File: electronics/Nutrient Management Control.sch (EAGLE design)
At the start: 28 parts, among them IC1 7407N, K1 SRM-1C-SL-5VDC, Q1 FQP30N06L, Q2 FQP30N06L, Q6 FDU3N40TU

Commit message: Just Microcontroller and control signals left todo
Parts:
- removed 24ACVS, IPUMP: (no value), Aeroponics Control:HEADER_POS2_43650-0215
- removed FM1, PS1: JST-XH-03-PIN-LONG-PAD, Aeroponics Control:JST-XH-03-PIN-LONG-PAD
- removed IPRSV, ISV: JST-XH-02-PIN-LONG-PAD, Aeroponics Control:JST-XH-02-PIN-LONG-PAD
- added C2, C3: 100n, Aeroponics Control:C-EU050-024X044
- added D10, D11, D12, D13, D14, D3, D4, D5, D7, D8, D9: 1N4004, Aeroponics Control:1N4004
- added DS4, DS5, ISEC: JST-XH-04-PIN-LONG-PAD, Aeroponics Control:JST-XH-04-PIN-LONG-PAD
- added HEAT, UV: (no value), Aeroponics Control:HEADER_POS2_43650-0215
- added IC2, IC3: 7407N, Aeroponics Control:7407N
- added K2: SRM-1C-SL-5VDC, Aeroponics Control:SRM-1C-SL-5VDC
- added MIXP, NP1, NP2, NP3, NP4, NP5, NP6, NP7, NP8, RORP, SUPP, WV: JST-XH-02-PIN-LONG-PAD, Aeroponics Control:JST-XH-02-PIN-LONG-PAD
- added Q10, Q11, Q12, Q13, Q3, Q4, Q5, Q7, Q8, Q9: FQP30N06L, Aeroponics Control:FQP30N06L
- added Q14: FDU3N40TU, Aeroponics Control:FDU3N40TU
- added R10, R13, R15, R17, R19, R21, R23, R25, R27, R3, R7: 10k, Aeroponics Control:R-EU_0204/7
- added R12, R14, R16, R18, R20, R22, R24, R26, R28, R4, R9: 1K, Aeroponics Control:R-EU_0204/7
- added TDS1, TDS2, TS1: JST-XH-03-PIN-LONG-PAD, Aeroponics Control:JST-XH-03-PIN-LONG-PAD
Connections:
- removed net +24VAC: 24ACVS.1, K1.COM
- removed net -24VAC: 24ACVS.2, IPUMP.1
- new net N$11: D4.A, NP3-2.S, Q4.D
- new net N$12: IC1C.O, R7.1, R9.1
- new net N$14: Q4.G, R9.2
- new net N$15: D5.A, NP5-2.S, Q5.D
- new net N$16: IC1E.O, R10.1, R12.1
- new net N$18: Q5.G, R12.2
- new net N$19: D7.A, NP7-2.S, Q7.D
- new net N$2: D3.A, NP1-2.S, Q3.D
- new net N$20: IC2A.O, R13.1, R14.1
- new net N$22: Q7.G, R14.2
- new net N$23: D8.A, NP2-2.S, Q8.D
- new net N$24: IC1B.O, R15.1, R16.1
- new net N$25: Q8.G, R16.2
- new net N$26: D9.A, NP4-2.S, Q9.D
- new net N$27: IC1D.O, R17.1, R18.1
- new net N$28: Q9.G, R18.2
- new net N$29: D10.A, NP6-2.S, Q10.D
- new net N$30: IC1F.O, R19.1, R20.1
- new net N$31: Q10.G, R20.2
- new net N$32: D11.A, NP8-2.S, Q11.D
- new net N$33: IC2B.O, R21.1, R22.1
- new net N$34: Q11.G, R22.2
- new net N$35: D12.A, Q12.D, RORP-2.S
- new net N$36: IC2E.O, R23.1, R24.1
- new net N$37: Q12.G, R24.2
- new net N$38: D13.A, Q13.D, WV-2.S
- new net N$39: IC2F.O, R25.1, R26.1
- new net N$40: Q13.G, R26.2
- new net N$41: D14.A, K2.COIL_1, Q14.D
- new net N$42: HEAT.2, K2.NO
- new net N$43: Q14.G, R28.2
- new net N$44: IC3B.O, R27.1, R28.1
- new net N$47: DS4-3.S
- new net N$48: DS4-4.S
- new net N$49: DS5-3.S
- new net N$50: DS5-4.S
- new net N$6: IC1A.O, R3.1, R4.1
- new net N$8: Q3.G, R4.2
- net +12V: now also D10.C, D11.C, D12.C, D13.C, D3.C, D4.C, D5.C, D7.C, D8.C, D9.C, MIXP-1.S, NP1-1.S, NP2-1.S, NP3-1.S, NP4-1.S, NP5-1.S, NP6-1.S, NP7-1.S, NP8-1.S, R27.2, RORP-1.S, SUPP-1.S, WV-1.S; no longer IPRSV-1.S, ISV-1.S
- net +240VAC: now also K1.COM, K2.COM
- net +5V: now also C2.1, C3.1, D14.C, DS4-1.S, DS5-1.S, IC2P.VCC, IC3P.VCC, K2.COIL_2, R10.2, R13.2, R15.2, R17.2, R19.2, R21.2, R23.2, R25.2, R3.2, R7.2, TDS1-1.S, TDS2-1.S, TS1-1.S; no longer FM1-1.S, PS1-1.S
- net -240VAC: now also HEAT.1, UV.1
- net DS1RX: no longer DS1-3.S
- net DS1TX: no longer DS1-4.S
- net DS2RX: no longer DS2-3.S
- net DS2TX: no longer DS2-4.S
- net DS3RX: no longer DS3-3.S
- net DS3TX: no longer DS3-4.S
- net FM1S: no longer FM1-3.S
- net GND: now also C2.2, C3.2, DS4-2.S, DS5-2.S, IC2P.GND, IC3P.GND, Q10.S, Q11.S, Q12.S, Q13.S, Q14.S, Q3.S, Q4.S, Q5.S, Q7.S, Q8.S, Q9.S, TDS1-2.S, TDS2-2.S, TS1-2.S; no longer FM1-2.S, PS1-2.S
- net IPCTL: no longer IC1E.I
- net IPRSVCTL: no longer IC1B.I
- net ISVCTL: no longer IC1A.I
- net N$1: now also MIXP-2.S; no longer IPRSV-2.S
- net N$10: now also SUPP-2.S; no longer ISV-2.S
- net N$17: now also IC3A.O; no longer IC1E.O
- net N$3: now also IC2D.O; no longer IC1A.O
- net N$7: now also UV.2; no longer IPUMP.2
- net N$9: now also IC2C.O; no longer IC1B.O
- net PS1S: no longer PS1-3.S
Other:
- note added: "Nutrient Pumps"
- note added: "Other Pumps and Valves"
- moved on the sheet: 12VS, 240ACVS, 5VS, C1, D1, D2, D6, DS1-1, DS1-2, DS1-3, DS1-4, DS2-1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

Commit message: First cut of Nutrient Management electronics
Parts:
- removed NP7: JST-XH-02-PIN-LONG-PAD, Aeroponics Control:JST-XH-02-PIN-LONG-PAD
- removed PCB1: ARDUINO_NANOARDUINO_NANO_HEADERS, Aeroponics Control:ARDUINO_NANO
- added PCB2: ARDUINO_MEGA2560_SHIELD, Aeroponics Control:ARDUINO_MEGA2560_SHIELD
- added PHDPP: JST-XH-02-PIN-LONG-PAD, Aeroponics Control:JST-XH-02-PIN-LONG-PAD
- renumbered NP8 to PHUPP
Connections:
- removed net DS1RX: PCB1.D2
- removed net DS1TX: PCB1.D3
- removed net DS2RX: PCB1.D4
- removed net DS2TX: PCB1.D5
- removed net DS3RX: PCB1.A5
- removed net DS3TX: PCB1.A4
- removed net FM1S: PCB1.A0
- removed net IPCTL: PCB1.D12
- removed net IPRSVCTL: PCB1.D7
- removed net ISVCTL: PCB1.D6
- removed net N$47: DS4-3.S
- removed net N$48: DS4-4.S
- removed net N$49: DS5-3.S
- removed net N$50: DS5-4.S
- removed net PS1S: PCB1.A7
- removed net TP1CTL: PCB1.D8
- removed net TP2CTL: PCB1.D9
- removed net UVLCTL: PCB1.D11
- new net HEATCTL: IC3B.I, PCB2.32
- new net MIXPCTL: IC2C.I, PCB2.2
- new net MTDO: DS1-4.S, PCB2.23
- new net MTT: PCB2.22, TS1-3.S
- new net N1PP: IC1A.I, PCB2.34
- new net N2PP: IC1B.I, PCB2.36
- new net N3PP: IC1C.I, PCB2.38
- new net N4PP: IC1D.I, PCB2.40
- new net N5PP: IC1E.I, PCB2.42
- new net N6PP: IC1F.I, PCB2.44
- new net PHDPP: IC2A.I, PCB2.46
- new net PHUPP: IC2B.I, PCB2.48
- new net RORPCTL: IC2E.I, PCB2.4
- new net RRTDO: DS3-4.S, PCB2.27
- new net STDO: DS2-4.S, PCB2.25
- new net SUPPCTL: IC2D.I, PCB2.3
- new net SWTDO: DS5-4.S, PCB2.31
- new net TDS1: PCB2.24, TDS1-3.S
- new net TDS2: PCB2.26, TDS2-3.S
- new net UVCTL: IC3A.I, PCB2.30
- new net WVCTL: IC2F.I, PCB2.49
- new net WWTDO: DS4-4.S, PCB2.29
- net +12V: now also PHDPP-1.S; no longer NP7-1.S
- net +5V: now also DS1-3.S, DS2-3.S, DS3-3.S, DS4-3.S, DS5-3.S, PCB2.AREF, PCB2.VIN; no longer PCB1.AREF, PCB1.VIN
- net GND: now also IC3C.I, IC3C.O, IC3D.I, IC3D.O, IC3E.I, IC3E.O, IC3F.I, IC3F.O, PCB2.GND; no longer PCB1.GND@1, PCB1.GND@2
- net N$19: now also PHDPP-2.S; no longer NP7-2.S
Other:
- moved on the sheet: 12VS, 240ACVS, 5VS, C1, C2, C3, D12, D2, D3, D4, D5, D7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

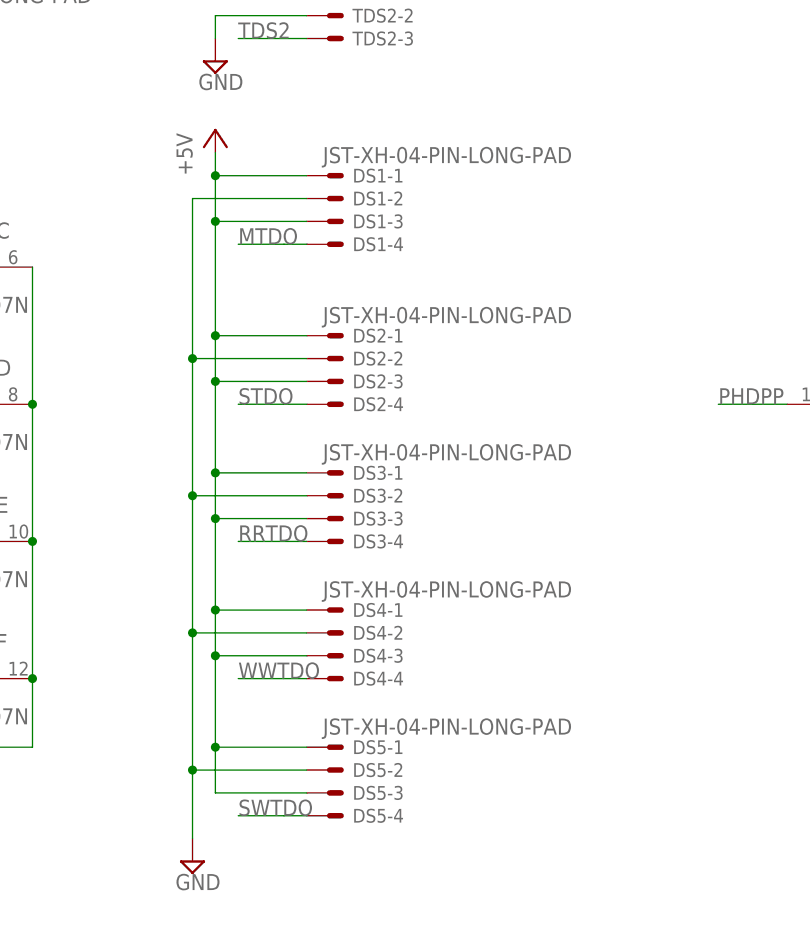
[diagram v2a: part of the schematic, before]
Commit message: First cut of Nutrient Management with multi UART breakout boards
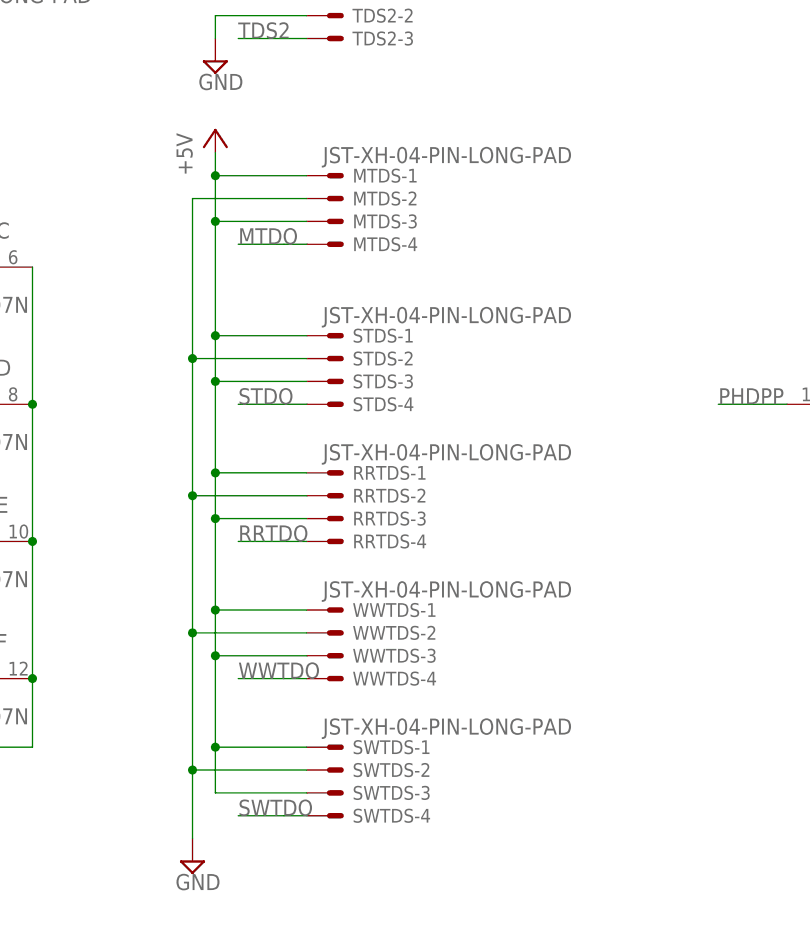
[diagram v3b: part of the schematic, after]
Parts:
- renumbered DS1 to MTDS, DS2 to STDS, DS3 to RRTDS, DS4 to WWTDS, DS5 to SWTDS
